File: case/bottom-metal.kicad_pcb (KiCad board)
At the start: 2 copper layers, 135 x 93.7 mm, 5 parts

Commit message: update case files
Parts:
- moved H1 2.80 mm to (104.8, 75.0)
- moved H2 2.80 mm to (175.8, 123.5)
- moved H3 2.80 mm to (84.8, 94.0)
- moved H4 2.80 mm to (124.2, 109.5)
- moved H5 2.80 mm to (162.2, 77.5)
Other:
- board size 135 x 93.7 mm -> 135 x 95.7 mm
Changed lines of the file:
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@@
       (drillshape 0)
       (scaleselection 1)
-      (outputdirectory "gerber/")
+      (outputdirectory "dxf/")
     )
   )
   (net 0 "")
   (footprint "kbd:thread_m2" (layer "F.Cu")
-    (at 178.5 123)
+    (at 175.75 123.5)
     (descr "Mounting Hole 2.2mm, no annular, M2")
     (tags "mounting hole 2.2mm no annular m2")
@@
   )
   (footprint "kbd:thread_m2" (layer "F.Cu")
-    (at 87.5 93.5)
+    (at 84.75 94)
     (descr "Mounting Hole 2.2mm, no annular, M2")
     (tags "mounting hole 2.2mm no annular m2")
@@
   )
   (footprint "kbd:thread_m2" (layer "F.Cu")
-    (at 165 77)
+    (at 124.25 109.5)
     (descr "Mounting Hole 2.2mm, no annular, M2")
     (tags "mounting hole 2.2mm no annular m2")
@@
     (property "Sheetname" "")
     (attr exclude_from_pos_files exclude_from_bom)
-    (fp_text reference "H5" (at -0.95 -0.55) (layer "F.Fab") hide
+    (fp_text reference "H4" (at -0.95 -0.55) (layer "F.Fab") hide
       (effects (font (size 1 1) (thickness 0.15)))
     )
@@
   )
   (footprint "kbd:thread_m2" (layer "F.Cu")
-    (at 107.5 74.5)
+    (at 104.75 75)
     (descr "Mounting Hole 2.2mm, no annular, M2")
     (tags "mounting hole 2.2mm no annular m2")
@@
   )
   (footprint "kbd:thread_m2" (layer "F.Cu")
-    (at 127 109)
+    (at 162.25 77.5)
     (descr "Mounting Hole 2.2mm, no annular, M2")
     (tags "mounting hole 2.2mm no annular m2")
@@
     (property "Sheetname" "")
     (attr exclude_from_pos_files exclude_from_bom)
-    (fp_text reference "H4" (at -0.95 -0.55) (layer "F.Fab") hide
+    (fp_text reference "H5" (at -0.95 -0.55) (layer "F.Fab") hide
       (effects (font (size 1 1) (thickness 0.15)))
     )
@@
     (pad "" np_thru_hole circle locked (at 0 0) (size 2.3 2.3) (drill 2.3) (layers *.Cu *.Mask))
   )
-  (gr_line (start 126 53) (end 126 53.5) (layer "Edge.Cuts") (width 0.1))
-  (gr_line (start 145 53.5) (end 145 53) (layer "Edge.Cuts") (width 0.1))
-  (gr_line (start 135 132.5) (end 154 132.5) (layer "Edge.Cuts") (width 0.1))
-  (gr_line (start 190.5 144) (end 203.5 121.5) (layer "Edge.Cuts") (width 0.1))
-  (gr_line (start 202 58) (end 165.5 58) (layer "Edge.Cuts") (width 0.1))
-  (gr_line (start 89.5 120.5) (end 107 120.5) (layer "Edge.Cuts") (width 0.1))
-  (gr_arc (start 86.5 112.5) (mid 87.56066 112.93934) (end 88 114) (layer "Edge.Cuts") (width 0.1))
-  (gr_line (start 87.5 65) (end 87.5 73) (layer "Edge.Cuts") (width 0.1))
-  (gr_arc (start 87.5 65) (mid 87.93934 63.93934) (end 89 63.5) (layer "Edge.Cuts") (width 0.1))
-  (gr_line (start 143.5 51.5) (end 127.5 51.5) (layer "Edge.Cuts") (width 0.1))
-  (gr_arc (start 106.5 62) (mid 106.06066 63.06066) (end 105 63.5) (layer "Edge.Cuts") (width 0.1))
-  (gr_line (start 107 120.5) (end 135 132.5) (layer "Edge.Cuts") (width 0.1))
-  (gr_arc (start 202 58) (mid 203.06066 58.43934) (end 203.5 59.5) (layer "Edge.Cuts") (width 0.1))
-  (gr_arc (start 68.5 76) (mid 68.93934 74.93934) (end 70 74.5) (layer "Edge.Cuts") (width 0.1))
-  (gr_line (start 203.5 121.5) (end 203.5 59.5) (layer "Edge.Cuts") (width 0.1))
-  (gr_line (start 108.5 55) (end 108 55) (layer "Edge.Cuts") (width 0.1))
-  (gr_arc (start 89.5 120.5) (mid 88.43934 120.06066) (end 88 119) (layer "Edge.Cuts") (width 0.1))
-  (gr_arc (start 165.5 58) (mid 164.43934 57.56066) (end 164 56.5) (layer "Edge.Cuts") (width 0.1))
-  (gr_arc (start 70 112.5) (mid 68.93934 112.06066) (end 68.5 111) (layer "Edge.Cuts") (width 0.1))
-  (gr_line (start 105 63.5) (end 89 63.5) (layer "Edge.Cuts") (width 0.1))
-  (gr_line (start 88 114) (end 88 119) (layer "Edge.Cuts") (width 0.1))
-  (gr_line (start 106.5 56.5) (end 106.5 62) (layer "Edge.Cuts") (width 0.1))
-  (gr_arc (start 190.5 144) (mid 187.849935 145.228185) (end 185.034016 144.452378) (layer "Edge.Cuts") (width 0.1))
-  (gr_line (start 124.5 55) (end 108.5 55) (layer "Edge.Cuts") (width 0.1))
-  (gr_arc (start 143.5 51.5) (mid 144.56066 51.93934) (end 145 53) (layer "Edge.Cuts") (width 0.1))
-  (gr_line (start 86 74.5) (end 70 74.5) (layer "Edge.Cuts") (width 0.1))
-  (gr_arc (start 87.5 73) (mid 87.06066 74.06066) (end 86 74.5) (layer "Edge.Cuts") (width 0.1))
-  (gr_arc (start 146.5 55) (mid 145.43934 54.56066) (end 145 53.5) (layer "Edge.Cuts") (width 0.1))
-  (gr_arc (start 126 53.5) (mid 125.56066 54.56066) (end 124.5 55) (layer "Edge.Cuts") (width 0.1))
-  (gr_arc (start 126 53) (mid 126.43934 51.93934) (end 127.5 51.5) (layer "Edge.Cuts") (width 0.1))
-  (gr_line (start 70 112.5) (end 86.5 112.5) (layer "Edge.Cuts") (width 0.1))
-  (gr_arc (start 162.5 55) (mid 163.56066 55.43934) (end 164 56.5) (layer "Edge.Cuts") (width 0.1))
-  (gr_line (start 185.034016 144.452378) (end 172.5 137.5) (layer "Edge.Cuts") (width 0.1))
-  (gr_line (start 162.5 55) (end 146.5 55) (layer "Edge.Cuts") (width 0.1))
-  (gr_arc (start 106.5 56.5) (mid 106.93934 55.43934) (end 108 55) (layer "Edge.Cuts") (width 0.1))
-  (gr_line (start 68.5 76) (end 68.5 111) (layer "Edge.Cuts") (width 0.1))
-  (gr_line (start 154 132.5) (end 172.5 137.5) (layer "Edge.Cuts") (width 0.1))
+  (gr_line (start 141.25 51.5) (end 124.25 51.5) (layer "Edge.Cuts") (width 0.1))
+  (gr_arc (start 84.75 65) (mid 85.18934 63.93934) (end 86.25 63.5) (layer "Edge.Cuts") (width 0.1))
+  (gr_arc (start 83.25 113.5) (mid 84.31066 113.93934) (end 84.75 115) (layer "Edge.Cuts") (width 0.1))
+  (gr_arc (start 144.25 55.5) (mid 143.18934 55.06066) (end 142.75 54) (layer "Edge.Cuts") (width 0.1))
+  (gr_line (start 86.25 121.5) (end 102.75 121.5) (layer "Edge.Cuts") (width 0.1))
+  (gr_line (start 103.75 57) (end 103.75 62) (layer "Edge.Cuts") (width 0.1))
+  (gr_arc (start 103.75 57) (mid 104.18934 55.93934) (end 105.25 55.5) (layer "Edge.Cuts") (width 0.1))
+  (gr_line (start 151.25 133) (end 169.75 138) (layer "Edge.Cuts") (width 0.1))
+  (gr_line (start 199.25 55.5) (end 144.25 55.5) (layer "Edge.Cuts") (width 0.1))
+  (gr_arc (start 199.25 55.5) (mid 200.31066 55.93934) (end 200.75 57) (layer "Edge.Cuts") (width 0.1))
+  (gr_arc (start 67.25 113.5) (mid 66.18934 113.06066) (end 65.75 112) (layer "Edge.Cuts") (width 0.1))
+  (gr_line (start 102.25 63.5) (end 86.25 63.5) (layer "Edge.Cuts") (width 0.1))
+  (gr_line (start 200.75 123) (end 200.75 57) (layer "Edge.Cuts") (width 0.1))
+  (gr_line (start 185.25 147) (end 169.75 138) (layer "Edge.Cuts") (width 0.1))
+  (gr_line (start 121.25 55.5) (end 105.25 55.5) (layer "Edge.Cuts") (width 0.1))
+  (gr_line (start 187.299038 146.450962) (end 200.75 123) (layer "Edge.Cuts") (width 0.1))
+  (gr_line (start 84.75 65) (end 84.75 73) (layer "Edge.Cuts") (width 0.1))
+  (gr_line (start 132.25 133) (end 151.25 133) (layer "Edge.Cuts") (width 0.1))
+  (gr_arc (start 84.75 73) (mid 84.31066 74.06066) (end 83.25 74.5) (layer "Edge.Cuts") (width 0.1))
+  (gr_line (start 67.25 113.5) (end 83.25 113.5) (layer "Edge.Cuts") (width 0.1))
+  (gr_arc (start 86.25 121.5) (mid 85.18934 121.06066) (end 84.75 120) (layer "Edge.Cuts") (width 0.1))
+  (gr_arc (start 141.25 51.5) (mid 142.31066 51.93934) (end 142.75 53) (layer "Edge.Cuts") (width 0.1))
+  (gr_arc (start 187.299038 146.450962) (mid 186.388233 147.149868) (end 185.25 147) (layer "Edge.Cuts") (width 0.1))
+  (gr_line (start 122.75 53) (end 122.75 54) (layer "Edge.Cuts") (width 0.1))
+  (gr_line (start 83.25 74.5) (end 67.25 74.5) (layer "Edge.Cuts") (width 0.1))
+  (gr_line (start 65.75 76) (end 65.75 112) (layer "Edge.Cuts") (width 0.1))
+  (gr_arc (start 103.75 62) (mid 103.31066 63.06066) (end 102.25 63.5) (layer "Edge.Cuts") (width 0.1))
+  (gr_line (start 102.75 121.5) (end 132.25 133) (layer "Edge.Cuts") (width 0.1))
+  (gr_arc (start 122.75 53) (mid 123.18934 51.93934) (end 124.25 51.5) (layer "Edge.Cuts") (width 0.1))
+  (gr_line (start 84.75 115) (end 84.75 120) (layer "Edge.Cuts") (width 0.1))
+  (gr_line (start 142.75 54) (end 142.75 53) (layer "Edge.Cuts") (width 0.1))
+  (gr_arc (start 122.75 54) (mid 122.31066 55.06066) (end 121.25 55.5) (layer "Edge.Cuts") (width 0.1))
+  (gr_arc (start 65.75 76) (mid 66.18934 74.93934) (end 67.25 74.5) (layer "Edge.Cuts") (width 0.1))
 )

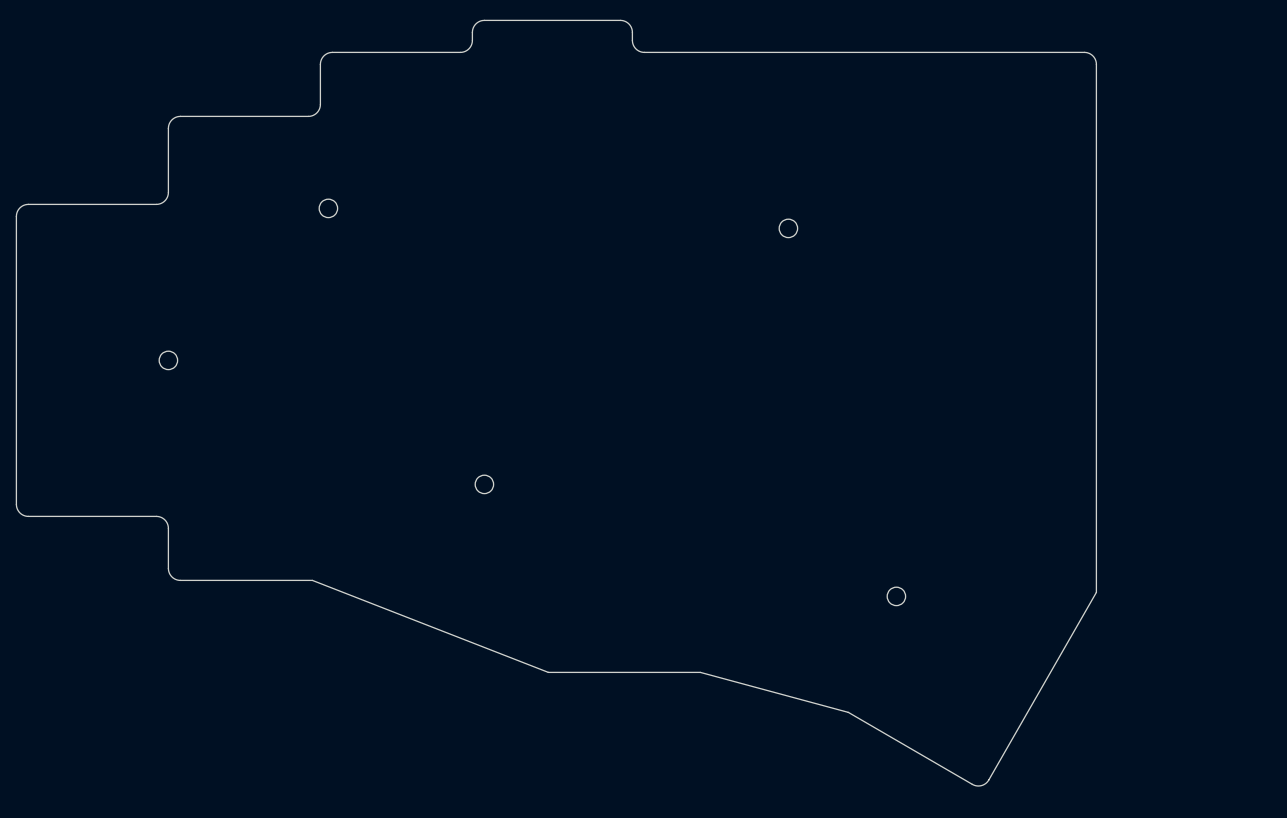
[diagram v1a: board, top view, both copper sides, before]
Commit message: update cases, extra hole on right side
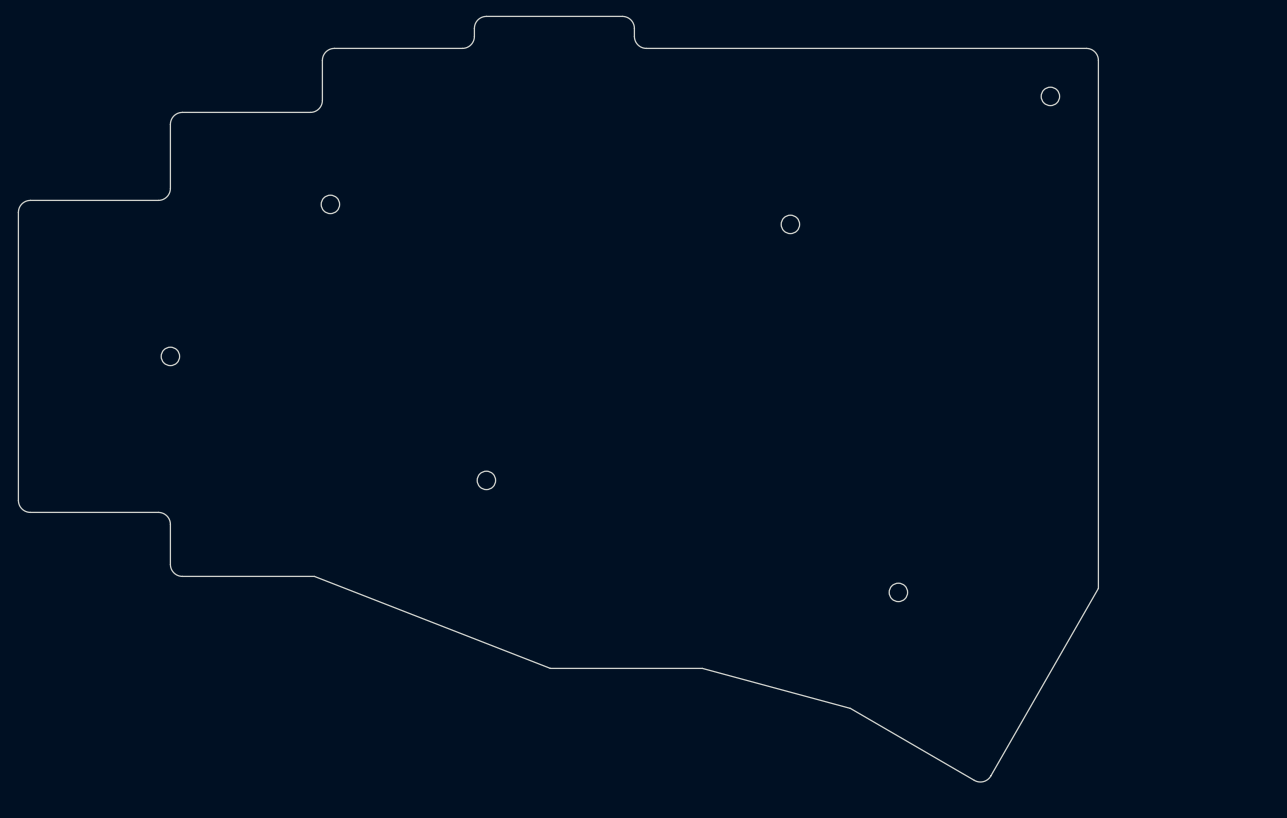
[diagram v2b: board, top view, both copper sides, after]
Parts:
- added H5: MountingHole, kbd:thread_m2, F.Cu at (195.0, 61.0)
- moved H1 0.56 mm to (105.0, 74.5)
- moved H2 0.56 mm to (176.0, 123.0)
- moved H3 0.56 mm to (85.0, 93.5)
- moved H4 0.56 mm to (124.5, 109.0)
- moved H5 0.56 mm to (162.5, 77.0)
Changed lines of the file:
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@@
   (net 0 "")
   (footprint "kbd:thread_m2" (layer "F.Cu")
-    (at 175.75 123.5)
+    (at 195 61)
+    (descr "Mounting Hole 2.2mm, no annular, M2")
+    (tags "mounting hole 2.2mm no annular m2")
+    (property "Sheetfile" "pica40.kicad_sch")
+    (property "Sheetname" "")
+    (attr exclude_from_pos_files exclude_from_bom)
+    (fp_text reference "H5" (at -0.95 -0.55) (layer "F.Fab") hide
+      (effects (font (size 1 1) (thickness 0.15)))
+    )
+    (fp_text value "MountingHole" (at 0 0.55) (layer "F.Fab") hide
+      (effects (font (size 1 1) (thickness 0.15)))
+    )
+    (pad "" np_thru_hole circle locked (at 0 0) (size 2.3 2.3) (drill 2.3) (layers *.Cu *.Mask))
+  )
+  (footprint "kbd:thread_m2" (layer "F.Cu")
+    (at 176 123)
     (descr "Mounting Hole 2.2mm, no annular, M2")
     (tags "mounting hole 2.2mm no annular m2")
@@
   )
   (footprint "kbd:thread_m2" (layer "F.Cu")
-    (at 84.75 94)
+    (at 85 93.5)
     (descr "Mounting Hole 2.2mm, no annular, M2")
     (tags "mounting hole 2.2mm no annular m2")
@@
   )
   (footprint "kbd:thread_m2" (layer "F.Cu")
-    (at 124.25 109.5)
+    (at 124.5 109)
     (descr "Mounting Hole 2.2mm, no annular, M2")
     (tags "mounting hole 2.2mm no annular m2")
@@
   )
   (footprint "kbd:thread_m2" (layer "F.Cu")
-    (at 104.75 75)
+    (at 105 74.5)
     (descr "Mounting Hole 2.2mm, no annular, M2")
     (tags "mounting hole 2.2mm no annular m2")
@@
   )
   (footprint "kbd:thread_m2" (layer "F.Cu")
-    (at 162.25 77.5)
+    (at 162.5 77)
     (descr "Mounting Hole 2.2mm, no annular, M2")
     (tags "mounting hole 2.2mm no annular m2")
@@
     (pad "" np_thru_hole circle locked (at 0 0) (size 2.3 2.3) (drill 2.3) (layers *.Cu *.Mask))
   )
-  (gr_line (start 141.25 51.5) (end 124.25 51.5) (layer "Edge.Cuts") (width 0.1))
-  (gr_arc (start 84.75 65) (mid 85.18934 63.93934) (end 86.25 63.5) (layer "Edge.Cuts") (width 0.1))
-  (gr_arc (start 83.25 113.5) (mid 84.31066 113.93934) (end 84.75 115) (layer "Edge.Cuts") (width 0.1))
-  (gr_arc (start 144.25 55.5) (mid 143.18934 55.06066) (end 142.75 54) (layer "Edge.Cuts") (width 0.1))
-  (gr_line (start 86.25 121.5) (end 102.75 121.5) (layer "Edge.Cuts") (width 0.1))
-  (gr_line (start 103.75 57) (end 103.75 62) (layer "Edge.Cuts") (width 0.1))
-  (gr_arc (start 103.75 57) (mid 104.18934 55.93934) (end 105.25 55.5) (layer "Edge.Cuts") (width 0.1))
-  (gr_line (start 151.25 133) (end 169.75 138) (layer "Edge.Cuts") (width 0.1))
-  (gr_line (start 199.25 55.5) (end 144.25 55.5) (layer "Edge.Cuts") (width 0.1))
-  (gr_arc (start 199.25 55.5) (mid 200.31066 55.93934) (end 200.75 57) (layer "Edge.Cuts") (width 0.1))
-  (gr_arc (start 67.25 113.5) (mid 66.18934 113.06066) (end 65.75 112) (layer "Edge.Cuts") (width 0.1))
-  (gr_line (start 102.25 63.5) (end 86.25 63.5) (layer "Edge.Cuts") (width 0.1))
-  (gr_line (start 200.75 123) (end 200.75 57) (layer "Edge.Cuts") (width 0.1))
-  (gr_line (start 185.25 147) (end 169.75 138) (layer "Edge.Cuts") (width 0.1))
-  (gr_line (start 121.25 55.5) (end 105.25 55.5) (layer "Edge.Cuts") (width 0.1))
-  (gr_line (start 187.299038 146.450962) (end 200.75 123) (layer "Edge.Cuts") (width 0.1))
-  (gr_line (start 84.75 65) (end 84.75 73) (layer "Edge.Cuts") (width 0.1))
-  (gr_line (start 132.25 133) (end 151.25 133) (layer "Edge.Cuts") (width 0.1))
-  (gr_arc (start 84.75 73) (mid 84.31066 74.06066) (end 83.25 74.5) (layer "Edge.Cuts") (width 0.1))
-  (gr_line (start 67.25 113.5) (end 83.25 113.5) (layer "Edge.Cuts") (width 0.1))
-  (gr_arc (start 86.25 121.5) (mid 85.18934 121.06066) (end 84.75 120) (layer "Edge.Cuts") (width 0.1))
-  (gr_arc (start 141.25 51.5) (mid 142.31066 51.93934) (end 142.75 53) (layer "Edge.Cuts") (width 0.1))
-  (gr_arc (start 187.299038 146.450962) (mid 186.388233 147.149868) (end 185.25 147) (layer "Edge.Cuts") (width 0.1))
-  (gr_line (start 122.75 53) (end 122.75 54) (layer "Edge.Cuts") (width 0.1))
-  (gr_line (start 83.25 74.5) (end 67.25 74.5) (layer "Edge.Cuts") (width 0.1))
-  (gr_line (start 65.75 76) (end 65.75 112) (layer "Edge.Cuts") (width 0.1))
-  (gr_arc (start 103.75 62) (mid 103.31066 63.06066) (end 102.25 63.5) (layer "Edge.Cuts") (width 0.1))
-  (gr_line (start 102.75 121.5) (end 132.25 133) (layer "Edge.Cuts") (width 0.1))
-  (gr_arc (start 122.75 53) (mid 123.18934 51.93934) (end 124.25 51.5) (layer "Edge.Cuts") (width 0.1))
-  (gr_line (start 84.75 115) (end 84.75 120) (layer "Edge.Cuts") (width 0.1))
-  (gr_line (start 142.75 54) (end 142.75 53) (layer "Edge.Cuts") (width 0.1))
-  (gr_arc (start 122.75 54) (mid 122.31066 55.06066) (end 121.25 55.5) (layer "Edge.Cuts") (width 0.1))
-  (gr_arc (start 65.75 76) (mid 66.18934 74.93934) (end 67.25 74.5) (layer "Edge.Cuts") (width 0.1))
+  (gr_line (start 141.5 51) (end 124.5 51) (layer "Edge.Cuts") (width 0.1))
+  (gr_arc (start 85 64.5) (mid 85.43934 63.43934) (end 86.5 63) (layer "Edge.Cuts") (width 0.1))
+  (gr_arc (start 83.5 113) (mid 84.56066 113.43934) (end 85 114.5) (layer "Edge.Cuts") (width 0.1))
+  (gr_arc (start 144.5 55) (mid 143.43934 54.56066) (end 143 53.5) (layer "Edge.Cuts") (width 0.1))
+  (gr_line (start 86.5 121) (end 103 121) (layer "Edge.Cuts") (width 0.1))
+  (gr_line (start 104 56.5) (end 104 61.5) (layer "Edge.Cuts") (width 0.1))
+  (gr_arc (start 104 56.5) (mid 104.43934 55.43934) (end 105.5 55) (layer "Edge.Cuts") (width 0.1))
+  (gr_line (start 151.5 132.5) (end 170 137.5) (layer "Edge.Cuts") (width 0.1))
+  (gr_line (start 199.5 55) (end 144.5 55) (layer "Edge.Cuts") (width 0.1))
+  (gr_arc (start 199.5 55) (mid 200.56066 55.43934) (end 201 56.5) (layer "Edge.Cuts") (width 0.1))
+  (gr_arc (start 67.5 113) (mid 66.43934 112.56066) (end 66 111.5) (layer "Edge.Cuts") (width 0.1))
+  (gr_line (start 102.5 63) (end 86.5 63) (layer "Edge.Cuts") (width 0.1))
+  (gr_line (start 201 122.5) (end 201 56.5) (layer "Edge.Cuts") (width 0.1))
+  (gr_line (start 185.5 146.5) (end 170 137.5) (layer "Edge.Cuts") (width 0.1))
+  (gr_line (start 121.5 55) (end 105.5 55) (layer "Edge.Cuts") (width 0.1))
+  (gr_line (start 187.549038 145.950962) (end 201 122.5) (layer "Edge.Cuts") (width 0.1))
+  (gr_line (start 85 64.5) (end 85 72.5) (layer "Edge.Cuts") (width 0.1))
+  (gr_line (start 132.5 132.5) (end 151.5 132.5) (layer "Edge.Cuts") (width 0.1))
+  (gr_arc (start 85 72.5) (mid 84.56066 73.56066) (end 83.5 74) (layer "Edge.Cuts") (width 0.1))
+  (gr_line (start 67.5 113) (end 83.5 113) (layer "Edge.Cuts") (width 0.1))
+  (gr_arc (start 86.5 121) (mid 85.43934 120.56066) (end 85 119.5) (layer "Edge.Cuts") (width 0.1))
+  (gr_arc (start 141.5 51) (mid 142.56066 51.43934) (end 143 52.5) (layer "Edge.Cuts") (width 0.1))
+  (gr_arc (start 187.549038 145.950962) (mid 186.63823 146.649869) (end 185.5 146.5) (layer "Edge.Cuts") (width 0.1))
+  (gr_line (start 123 52.5) (end 123 53.5) (layer "Edge.Cuts") (width 0.1))
+  (gr_line (start 83.5 74) (end 67.5 74) (layer "Edge.Cuts") (width 0.1))
+  (gr_line (start 66 75.5) (end 66 111.5) (layer "Edge.Cuts") (width 0.1))
+  (gr_arc (start 104 61.5) (mid 103.56066 62.56066) (end 102.5 63) (layer "Edge.Cuts") (width 0.1))
+  (gr_line (start 103 121) (end 132.5 132.5) (layer "Edge.Cuts") (width 0.1))
+  (gr_arc (start 123 52.5) (mid 123.43934 51.43934) (end 124.5 51) (layer "Edge.Cuts") (width 0.1))
+  (gr_line (start 85 114.5) (end 85 119.5) (layer "Edge.Cuts") (width 0.1))
+  (gr_line (start 143 53.5) (end 143 52.5) (layer "Edge.Cuts") (width 0.1))
+  (gr_arc (start 123 53.5) (mid 122.56066 54.56066) (end 121.5 55) (layer "Edge.Cuts") (width 0.1))
+  (gr_arc (start 66 75.5) (mid 66.43934 74.43934) (end 67.5 74) (layer "Edge.Cuts") (width 0.1))
 )

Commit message: update case files
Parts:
- removed the H5 at (195.0, 61.0)
- removed the H5 at (162.5, 77.0)
- added H5: MountingHole, kbd:thread_m2, F.Cu at (184.0, 79.5)
- added H6: MountingHole, kbd:thread_m2, F.Cu at (206.5, 86.5)
- added H7: MountingHole, kbd:thread_m2, F.Cu at (215.2, 86.5)
- moved H3 22.5 mm to (105.2, 103.2), turned to 5 degrees
- moved H2 21.6 mm to (197.5, 125.5)
- moved H4 21.6 mm to (146.0, 111.5)
- moved H1 20.0 mm to (124.8, 77.0)
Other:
- board size 135 x 95.7 mm -> 137.8 x 95.7 mm
